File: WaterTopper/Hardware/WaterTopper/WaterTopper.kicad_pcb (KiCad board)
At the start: 4 copper layers, 42.5 x 71 mm, 62 parts, among them J1 TYPE-C-31-M-12, J2 Barrel_Jack_Switch, J3 Conn_01x07, J4 Conn_01x04, J5 Conn_01x04, J6 Conn_01x04, J7 Conn_01x04, J8 Screw_Terminal_01x02, J9 Screw_Terminal_01x02, Q1 2N7002, SW1 SW_SPST, SW2 SW_SPST, U1 AP2112K-3.3, U2 ESP32-S3-MINI-1-N8, U3 DRV8881PRHRT, U4 BMP280

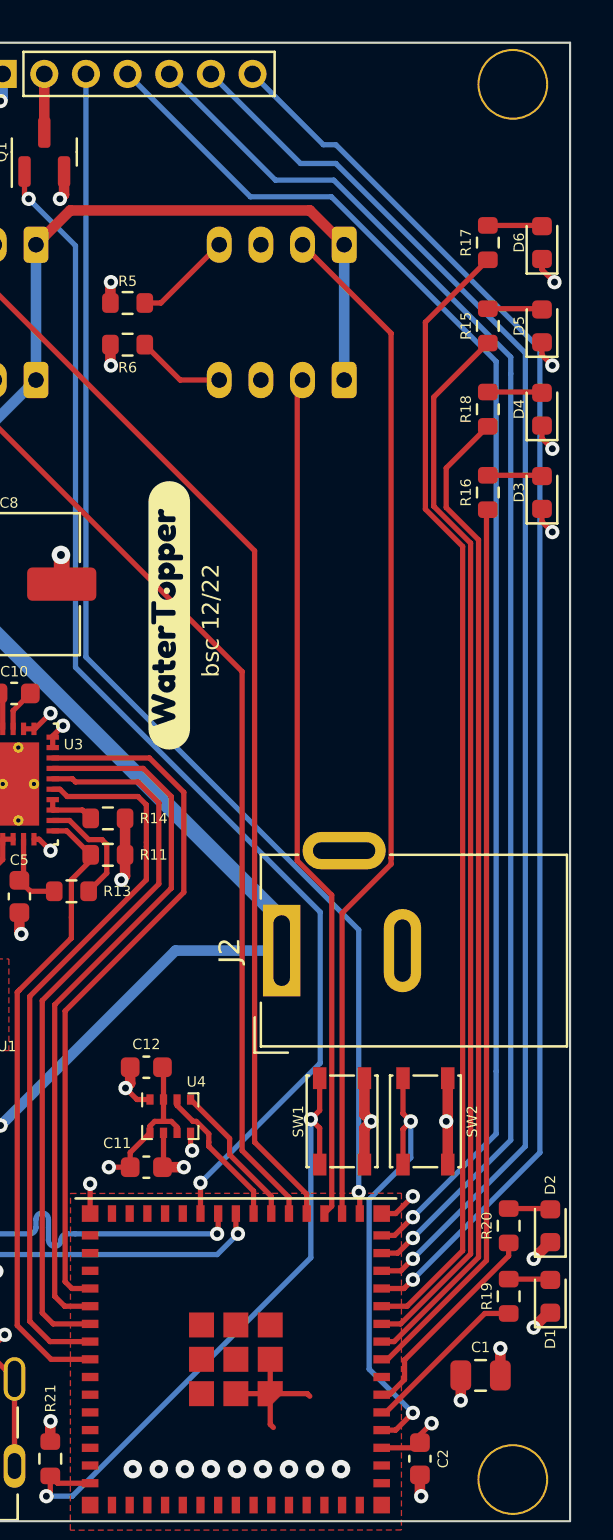
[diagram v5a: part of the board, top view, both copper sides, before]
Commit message: Added button
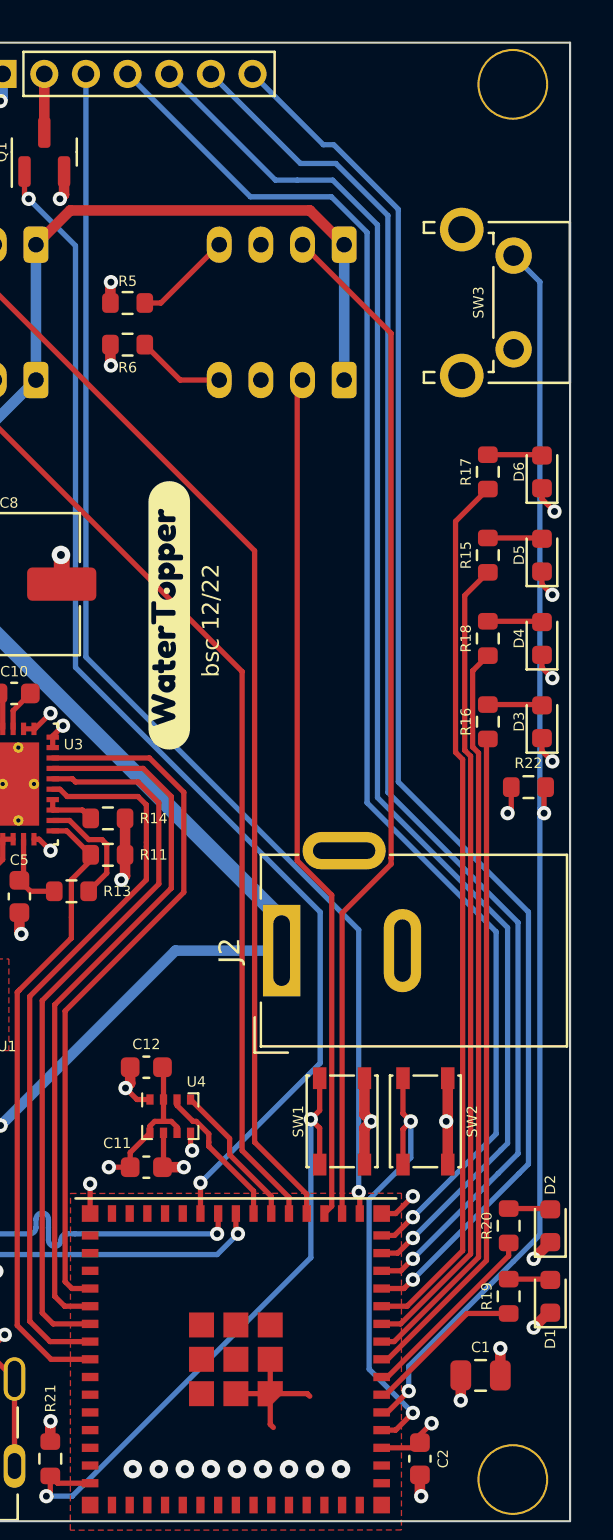
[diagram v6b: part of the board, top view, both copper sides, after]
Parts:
- added R22: 10k, Resistor_SMD:R_0603_1608Metric, F.Cu at (168.8, 90.8)
- added SW3: SW_SPST, Button_Switch_THT:SW_Tactile_SPST_Angled_PTS645Vx58-2LFS, F.Cu at (168.0, 65.2)
- moved D3 11.0 mm to (169.4, 87.6)
- moved D4 11.0 mm to (169.4, 83.6)
- moved D5 11.0 mm to (169.4, 79.6)
- moved D6 11.0 mm to (169.4, 75.6)
- moved R15 11.0 mm to (166.8, 79.6)
- moved R16 11.0 mm to (166.8, 87.6)
- moved R17 11.0 mm to (166.8, 75.6)
- moved R18 11.0 mm to (166.8, 83.6)
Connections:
- U2 pad 5: ULED_1 -> U_BTN
- U2 pad 6: ULED_2 -> ULED_1
- U2 pad 7: unconnected-(U2-Pad7) -> ULED_2
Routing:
- net U_BTN: track 0.00 -> 61.0 mm, vias 0 -> 2
- net ULED_5: track 51.2 -> 39.0 mm
- net ULED_6: track 54.6 -> 42.4 mm
- net ULED_4: track 47.7 -> 35.6 mm
- net ULED_3: track 43.1 -> 32.1 mm
- net ULED_2: track 10.5 -> 9.13 mm
- net +3V3: track 18.4 -> 19.8 mm, vias 15 -> 16
- net TFT_CS: track 68.2 -> 67.7 mm

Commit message: Added BOM, added voltage divider
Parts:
- added R23: 5k1, Resistor_SMD:R_0603_1608Metric, F.Cu at (134.0, 111.0)
- added R24: 5k1, Resistor_SMD:R_0603_1608Metric, F.Cu at (134.0, 107.8)
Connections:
- D8 pad 1: Net-(C3-Pad1) -> Net-(D8-Pad1)
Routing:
- net Net-(C3-Pad1): track 0.00 -> 5.19 mm
- net Net-(D8-Pad1): track 0.00 -> 3.41 mm
- net MTR2A: track 13.7 -> 14.8 mm
- net GND: track 72.6 -> 71.9 mm, vias 43 -> 48
- net MTR1A: track 13.5 -> 14.1 mm
